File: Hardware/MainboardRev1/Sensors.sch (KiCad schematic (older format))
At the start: 25 parts, among them J6 Stratologger_PWR, J7 Stratologger_DATA, Q25 SSM3J328R, Q26 NTR4003, U12 ABPMANN030PG2A3, U13 LSM9DS1, U14 LIS331HH, U15 BME280, U16 CCS811

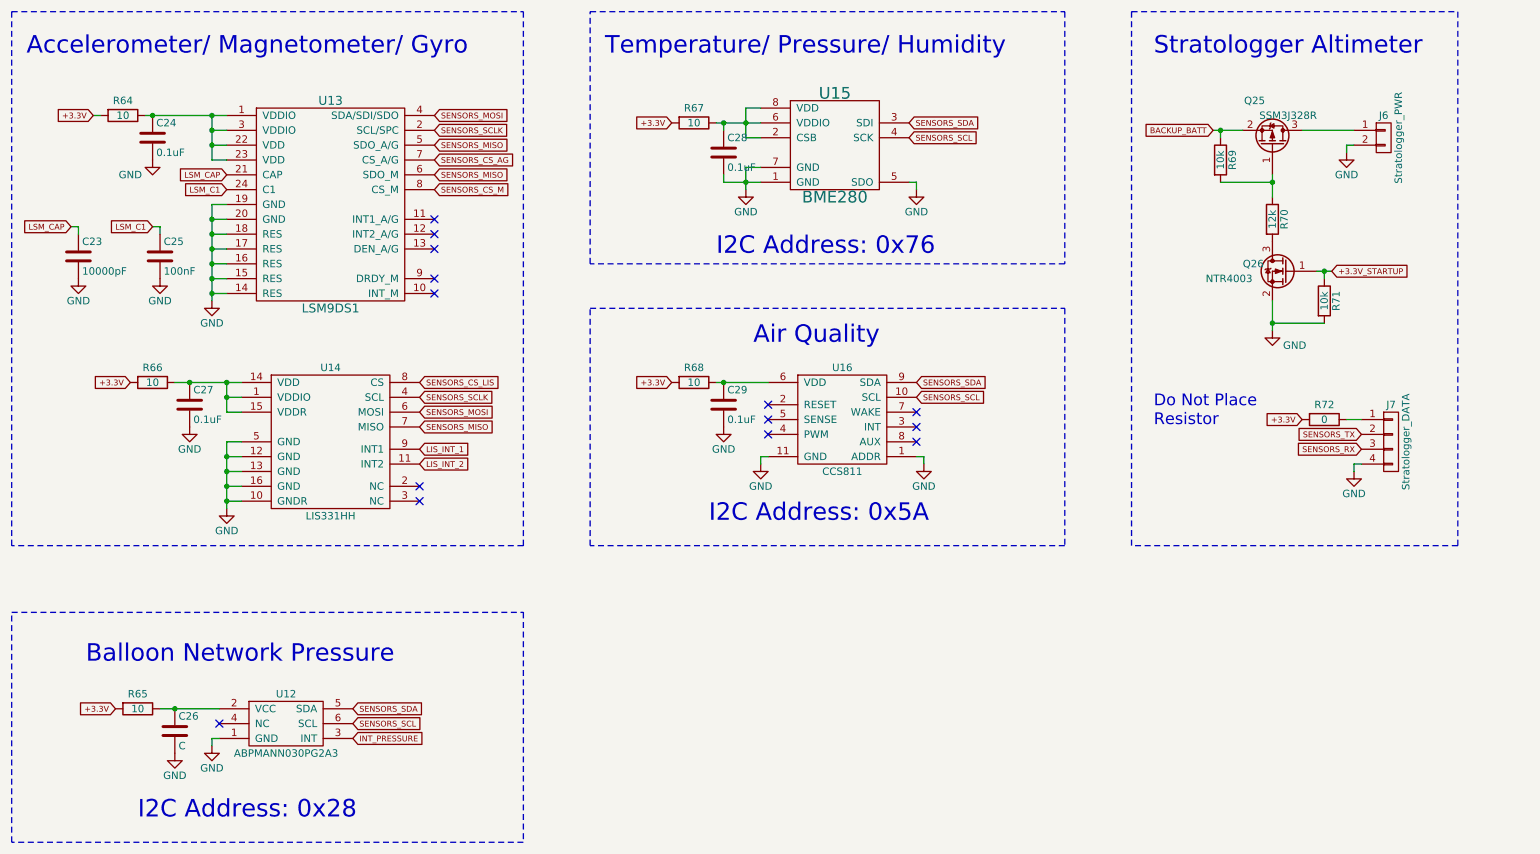
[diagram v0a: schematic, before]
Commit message: Small changes to schematic: Added voltage dividers for analog inputs, small net changes. Added footprints for each part
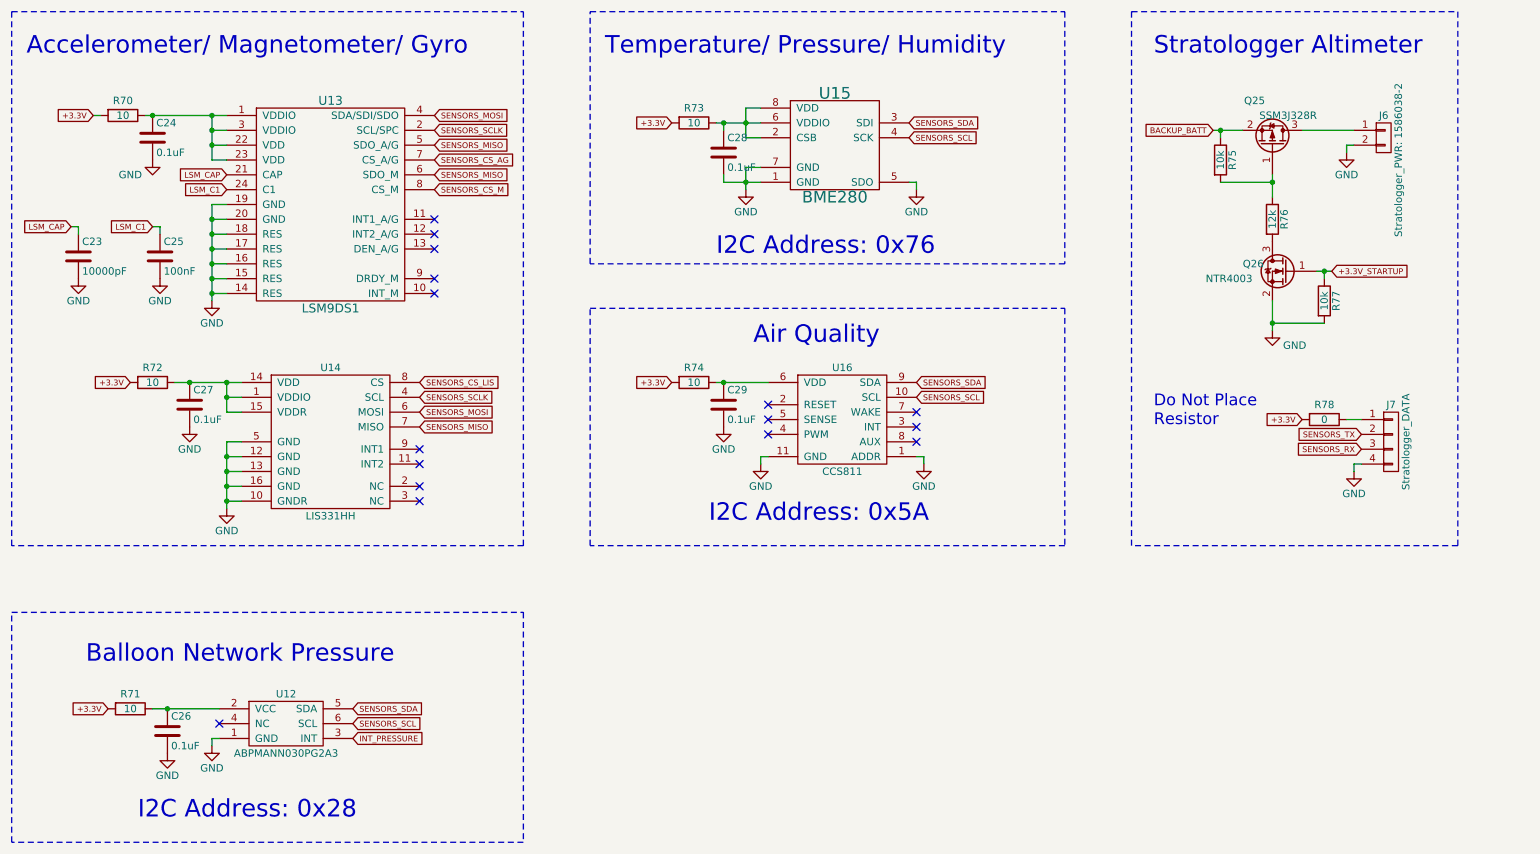
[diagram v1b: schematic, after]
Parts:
- C23, C24, C25, C27, C28, C29: footprint (none) -> Capacitors_SMD:C_0603_HandSoldering
- C26: value C -> 0.1uF; footprint (none) -> Capacitors_SMD:C_0603_HandSoldering
- J6: value Stratologger_PWR -> Stratologger_PWR: 1586038-2; footprint (none) -> Dans_Parts:CONN_2POS_VERT_TE_CONN
- J7: footprint (none) -> Dans_Parts:4-Pin_Molex_Vertical
- Q25, Q26: footprint (none) -> TO_SOT_Packages_SMD:SOT-23
- R70: renamed from R64; footprint (none) -> Resistors_SMD:R_0603_HandSoldering
- R71: renamed from R65; footprint (none) -> Resistors_SMD:R_0603_HandSoldering
- R72: renamed from R66; footprint (none) -> Resistors_SMD:R_0603_HandSoldering
- R73: renamed from R67; footprint (none) -> Resistors_SMD:R_0603_HandSoldering
- R74: renamed from R68; footprint (none) -> Resistors_SMD:R_0603_HandSoldering
- R75: renamed from R69; footprint (none) -> Resistors_SMD:R_0603_HandSoldering
- R76: renamed from R70; footprint (none) -> Resistors_SMD:R_0603_HandSoldering
- R77: renamed from R71; footprint (none) -> Resistors_SMD:R_0603_HandSoldering
- R78: renamed from R72; footprint (none) -> Resistors_SMD:R_0603_HandSoldering
- U12: footprint (none) -> Dans_Parts:PRESSURE_TRANSDUCER_ABPMANN030PG2A3
- U13: footprint (none) -> LSM9DS1:PQFN24P43_350X300X102L35X23N
- U14: footprint (none) -> Dans_Parts:LGA16_3x3mm_0.5mm_pitch
- U15: footprint (none) -> Dans_Parts:BME280
- U16: footprint (none) -> Dans_Parts:SON60P270X400X110-11N
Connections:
- net LIS_INT_1: no longer names the net of U14.9 (INT1)
- net LIS_INT_2: no longer names the net of U14.11 (INT2)
- no-connect marks 14 -> 16
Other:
- moved on the sheet: C26, R71

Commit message: Components placed. Needs to be routed.
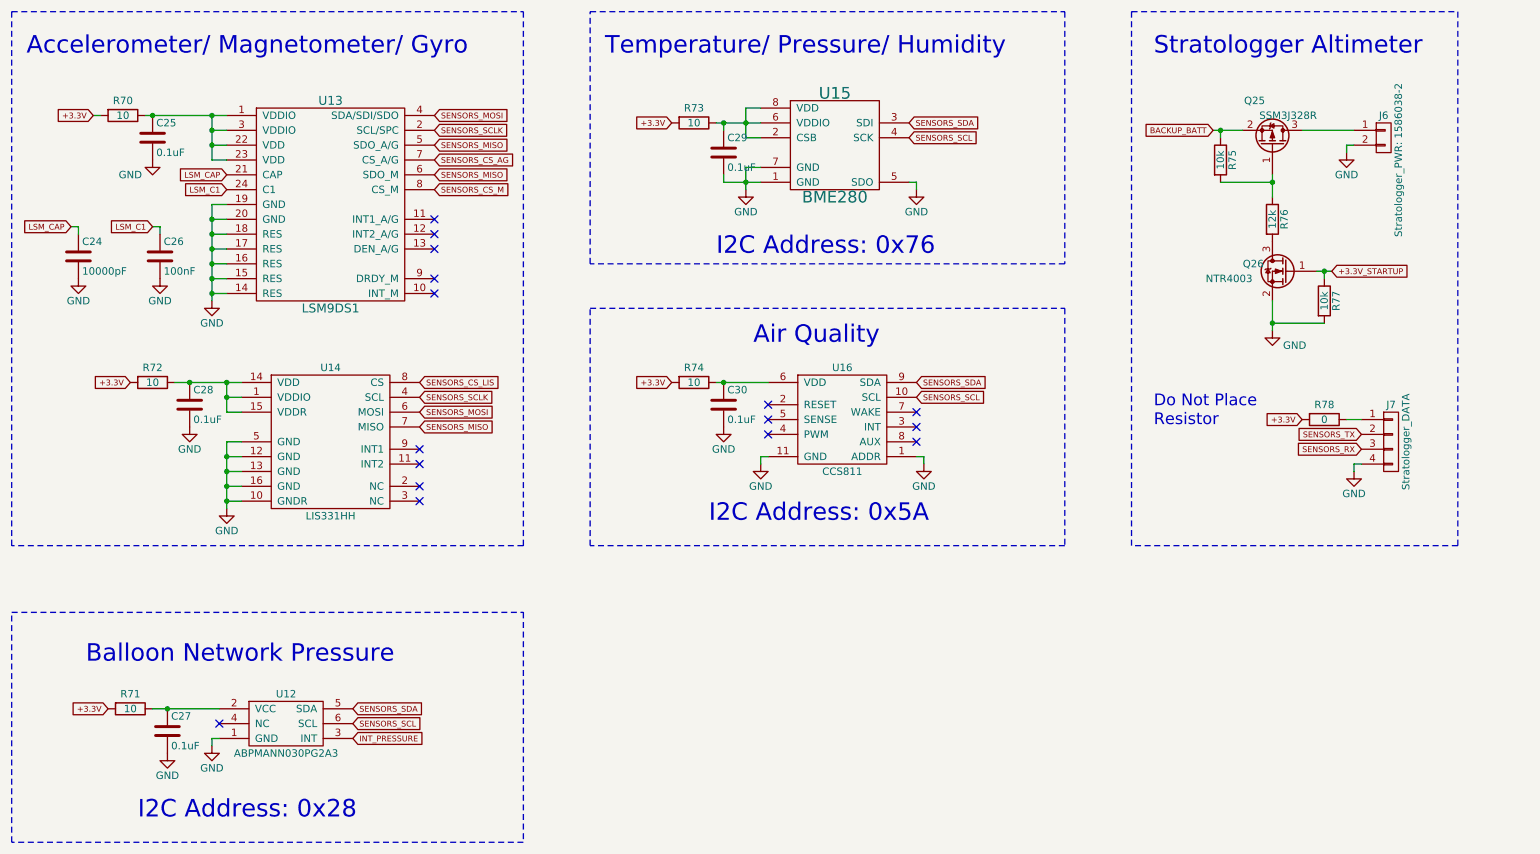
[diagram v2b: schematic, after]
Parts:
- renumbered C23 to C24, C24 to C25, C25 to C26, C26 to C27, C27 to C28, C28 to C29, C29 to C30
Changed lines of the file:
@@
 LIBS:teensy3_6-OuterHeadersOnly
 LIBS:switches
+LIBS:mounting_hole_eighth_inch
 LIBS:MainboardRev1-cache
 EELAYER 25 0
@@
 $EndComp
 $Comp
-L C C24
+L C C25
 U 1 1 5AFB84A4
 P 1950 2100
-F 0 "C24" H 1975 2200 50  0000 L CNN
+F 0 "C25" H 1975 2200 50  0000 L CNN
 F 1 "0.1uF" H 1975 2000 50  0000 L CNN
 F 2 "Capacitors_SMD:C_0603_HandSoldering" H 1988 1950 50  0001 C CNN
@@
 $EndComp
 $Comp
-L GND #PWR050
+L GND #PWR056
 U 1 1 5AFB852E
 P 1950 2250
-F 0 "#PWR050" H 1950 2000 50  0001 C CNN
+F 0 "#PWR056" H 1950 2000 50  0001 C CNN
 F 1 "GND" H 1800 2150 50  0000 C CNN
 F 2 "" H 1950 2250 50  0001 C CNN
@@
 LSM_C1
 $Comp
-L GND #PWR051
+L GND #PWR057
 U 1 1 5AFB88C9
 P 2350 3200
-F 0 "#PWR051" H 2350 2950 50  0001 C CNN
+F 0 "#PWR057" H 2350 2950 50  0001 C CNN
 F 1 "GND" H 2350 3050 50  0000 C CNN
 F 2 "" H 2350 3200 50  0001 C CNN
@@
 $EndComp
 $Comp
-L C C23
+L C C24
 U 1 1 5AFB8B0C
 P 1450 2900
-F 0 "C23" H 1475 3000 50  0000 L CNN
+F 0 "C24" H 1475 3000 50  0000 L CNN
 F 1 "10000pF" H 1475 2800 50  0000 L CNN
 F 2 "Capacitors_SMD:C_0603_HandSoldering" H 1488 2750 50  0001 C CNN
@@
 $EndComp
 $Comp
-L C C25
+L C C26
 U 1 1 5AFB8B41
 P 2000 2900
-F 0 "C25" H 2025 3000 50  0000 L CNN
+F 0 "C26" H 2025 3000 50  0000 L CNN
 F 1 "100nF" H 2025 2800 50  0000 L CNN
 F 2 "Capacitors_SMD:C_0603_HandSoldering" H 2038 2750 50  0001 C CNN
@@
 $EndComp
 $Comp
-L GND #PWR052
+L GND #PWR058
 U 1 1 5AFB8B74
 P 1450 3050
-F 0 "#PWR052" H 1450 2800 50  0001 C CNN
+F 0 "#PWR058" H 1450 2800 50  0001 C CNN
 F 1 "GND" H 1450 2900 50  0000 C CNN
 F 2 "" H 1450 3050 50  0001 C CNN
@@
 $EndComp
 $Comp
-L GND #PWR053
+L GND #PWR059
 U 1 1 5AFB8B92
 P 2000 3050
-F 0 "#PWR053" H 2000 2800 50  0001 C CNN
+F 0 "#PWR059" H 2000 2800 50  0001 C CNN
 F 1 "GND" H 2000 2900 50  0000 C CNN
 F 2 "" H 2000 3050 50  0001 C CNN
@@
 $EndComp
 $Comp
-L GND #PWR054
+L GND #PWR060
 U 1 1 5AFB9518
 P 7100 2450
-F 0 "#PWR054" H 7100 2200 50  0001 C CNN
+F 0 "#PWR060" H 7100 2200 50  0001 C CNN
 F 1 "GND" H 7100 2300 50  0000 C CNN
 F 2 "" H 7100 2450 50  0001 C CNN
@@
 $EndComp
 $Comp
-L GND #PWR055
+L GND #PWR061
 U 1 1 5AFB95E4
 P 5950 2450
-F 0 "#PWR055" H 5950 2200 50  0001 C CNN
+F 0 "#PWR061" H 5950 2200 50  0001 C CNN
 F 1 "GND" H 5950 2300 50  0000 C CNN
 F 2 "" H 5950 2450 50  0001 C CNN
@@
 $EndComp
 $Comp
-L C C28
+L C C29
 U 1 1 5AFB983D
 P 5800 2200
-F 0 "C28" H 5825 2300 50  0000 L CNN
+F 0 "C29" H 5825 2300 50  0000 L CNN
 F 1 "0.1uF" H 5825 2100 50  0000 L CNN
 F 2 "Capacitors_SMD:C_0603_HandSoldering" H 5838 2050 50  0001 C CNN
@@
 NoConn ~ 3750 4450
 $Comp
-L GND #PWR056
+L GND #PWR062
 U 1 1 5AFBAE49
 P 2450 4600
-F 0 "#PWR056" H 2450 4350 50  0001 C CNN
+F 0 "#PWR062" H 2450 4350 50  0001 C CNN
 F 1 "GND" H 2450 4450 50  0000 C CNN
 F 2 "" H 2450 4600 50  0001 C CNN
@@
 $EndComp
 $Comp
-L C C27
+L C C28
 U 1 1 5AFBB438
 P 2200 3900
-F 0 "C27" H 2225 4000 50  0000 L CNN
+F 0 "C28" H 2225 4000 50  0000 L CNN
 F 1 "0.1uF" H 2225 3800 50  0000 L CNN
 F 2 "Capacitors_SMD:C_0603_HandSoldering" H 2238 3750 50  0001 C CNN
@@
 $EndComp
 $Comp
-L GND #PWR057
+L GND #PWR063
 U 1 1 5AFBB46D
 P 2200 4050
-F 0 "#PWR057" H 2200 3800 50  0001 C CNN
+F 0 "#PWR063" H 2200 3800 50  0001 C CNN
 F 1 "GND" H 2200 3900 50  0000 C CNN
 F 2 "" H 2200 4050 50  0001 C CNN
@@
 NoConn ~ 6100 4100
 $Comp
-L C C29
+L C C30
 U 1 1 5AFBC423
 P 5800 3900
-F 0 "C29" H 5825 4000 50  0000 L CNN
+F 0 "C30" H 5825 4000 50  0000 L CNN
 F 1 "0.1uF" H 5825 3800 50  0000 L CNN
 F 2 "Capacitors_SMD:C_0603_HandSoldering" H 5838 3750 50  0001 C CNN
@@
 +3.3V
 $Comp
-L GND #PWR058
+L GND #PWR064
 U 1 1 5AFBC6D4
 P 5800 4050
-F 0 "#PWR058" H 5800 3800 50  0001 C CNN
+F 0 "#PWR064" H 5800 3800 50  0001 C CNN
 F 1 "GND" H 5800 3900 50  0000 C CNN
 F 2 "" H 5800 4050 50  0001 C CNN
@@
 $EndComp
 $Comp
-L GND #PWR059
+L GND #PWR065
 U 1 1 5AFBC95B
 P 6050 4300
-F 0 "#PWR059" H 6050 4050 50  0001 C CNN
+F 0 "#PWR065" H 6050 4050 50  0001 C CNN
 F 1 "GND" H 6050 4150 50  0000 C CNN
 F 2 "" H 6050 4300 50  0001 C CNN
@@
 SENSORS_SDA
 $Comp
-L GND #PWR060
+L GND #PWR066
 U 1 1 5AFBCEAE
 P 7150 4300
-F 0 "#PWR060" H 7150 4050 50  0001 C CNN
+F 0 "#PWR066" H 7150 4050 50  0001 C CNN
 F 1 "GND" H 7150 4150 50  0000 C CNN
 F 2 "" H 7150 4300 50  0001 C CNN
@@
 BACKUP_BATT
 $Comp
-L GND #PWR061
+L GND #PWR067
 U 1 1 5AFBEC0B
 P 10000 2200
-F 0 "#PWR061" H 10000 1950 50  0001 C CNN
+F 0 "#PWR067" H 10000 1950 50  0001 C CNN
 F 1 "GND" H 10000 2050 50  0000 C CNN
 F 2 "" H 10000 2200 50  0001 C CNN
@@
 $EndComp
 $Comp
-L GND #PWR062
+L GND #PWR068
 U 1 1 5AFBF3FF
 P 10050 4350
-F 0 "#PWR062" H 10050 4100 50  0001 C CNN
+F 0 "#PWR068" H 10050 4100 50  0001 C CNN
 F 1 "GND" H 10050 4200 50  0000 C CNN
 F 2 "" H 10050 4350 50  0001 C CNN
@@
 $EndComp
 $Comp
-L C C26
+L C C27
 U 1 1 5AFC1C18
 P 2050 6100
-F 0 "C26" H 2075 6200 50  0000 L CNN
+F 0 "C27" H 2075 6200 50  0000 L CNN
 F 1 "0.1uF" H 2075 6000 50  0000 L CNN
 F 2 "Capacitors_SMD:C_0603_HandSoldering" H 2088 5950 50  0001 C CNN
@@
 	1950 5950 2400 5950
 $Comp
-L GND #PWR063
+L GND #PWR069
 U 1 1 5AFC1CBA
 P 2050 6250
-F 0 "#PWR063" H 2050 6000 50  0001 C CNN
+F 0 "#PWR069" H 2050 6000 50  0001 C CNN
 F 1 "GND" H 2050 6100 50  0000 C CNN
 F 2 "" H 2050 6250 50  0001 C CNN
@@
 $EndComp
 $Comp
-L GND #PWR064
+L GND #PWR070
 U 1 1 5AFC1CF4
 P 2350 6200
-F 0 "#PWR064" H 2350 5950 50  0001 C CNN
+F 0 "#PWR070" H 2350 5950 50  0001 C CNN
 F 1 "GND" H 2350 6050 50  0000 C CNN
 F 2 "" H 2350 6200 50  0001 C CNN
@@
 $EndComp
 $Comp
-L GND #PWR065
+L GND #PWR071
 U 1 1 5B0149BF
 P 9500 3400
-F 0 "#PWR065" H 9500 3150 50  0001 C CNN
+F 0 "#PWR071" H 9500 3150 50  0001 C CNN
 F 1 "GND" H 9650 3300 50  0000 C CNN
 F 2 "" H 9500 3400 50  0000 C CNN
